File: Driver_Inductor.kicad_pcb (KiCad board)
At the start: 6 copper layers, 119.6 x 60.5 mm, 91 parts, among them J1 Control_A, J2 DC+, J3 DC-, J4 OUT1, J5 OUT2, Q1 IRLML2402TRPBF, U3 LM1117GS-5.0, U4 LMV7219M5, U5 ADuM1200AR

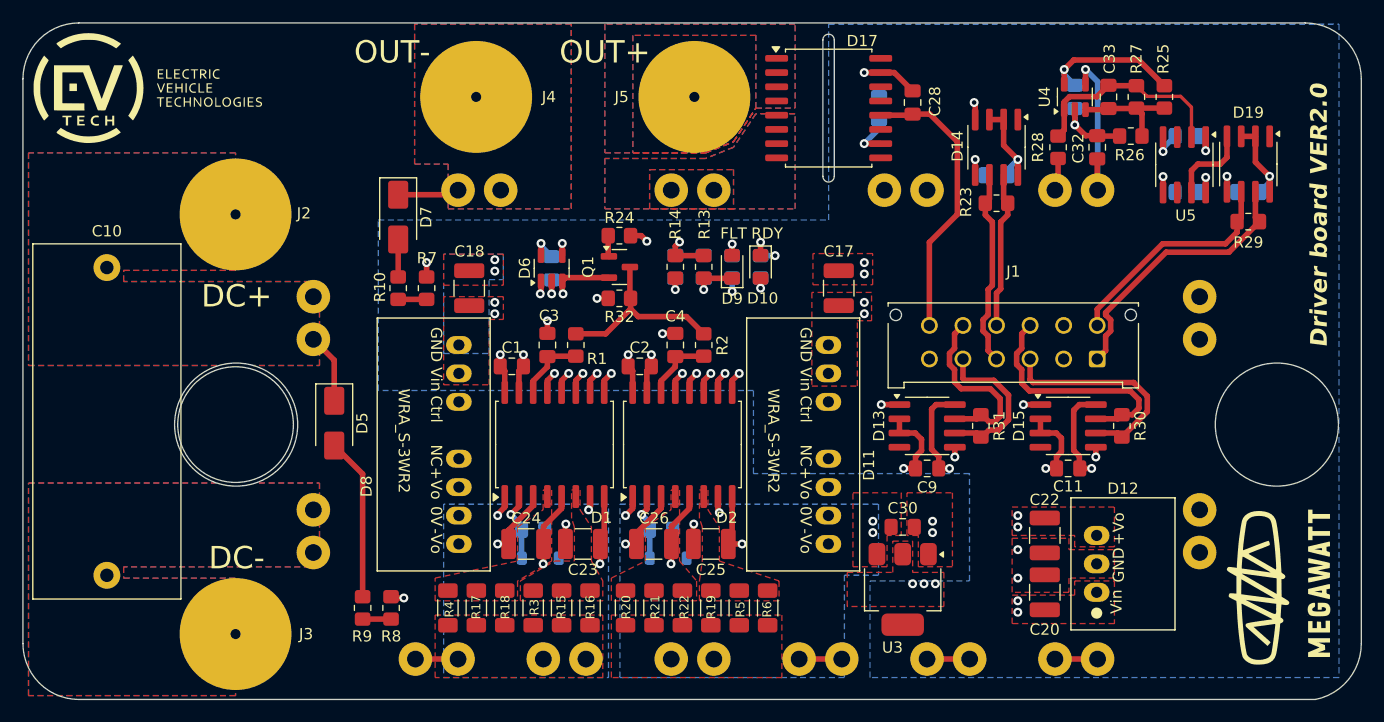
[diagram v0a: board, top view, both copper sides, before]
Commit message: VER2.1: внес все исправления для заказа в Китае
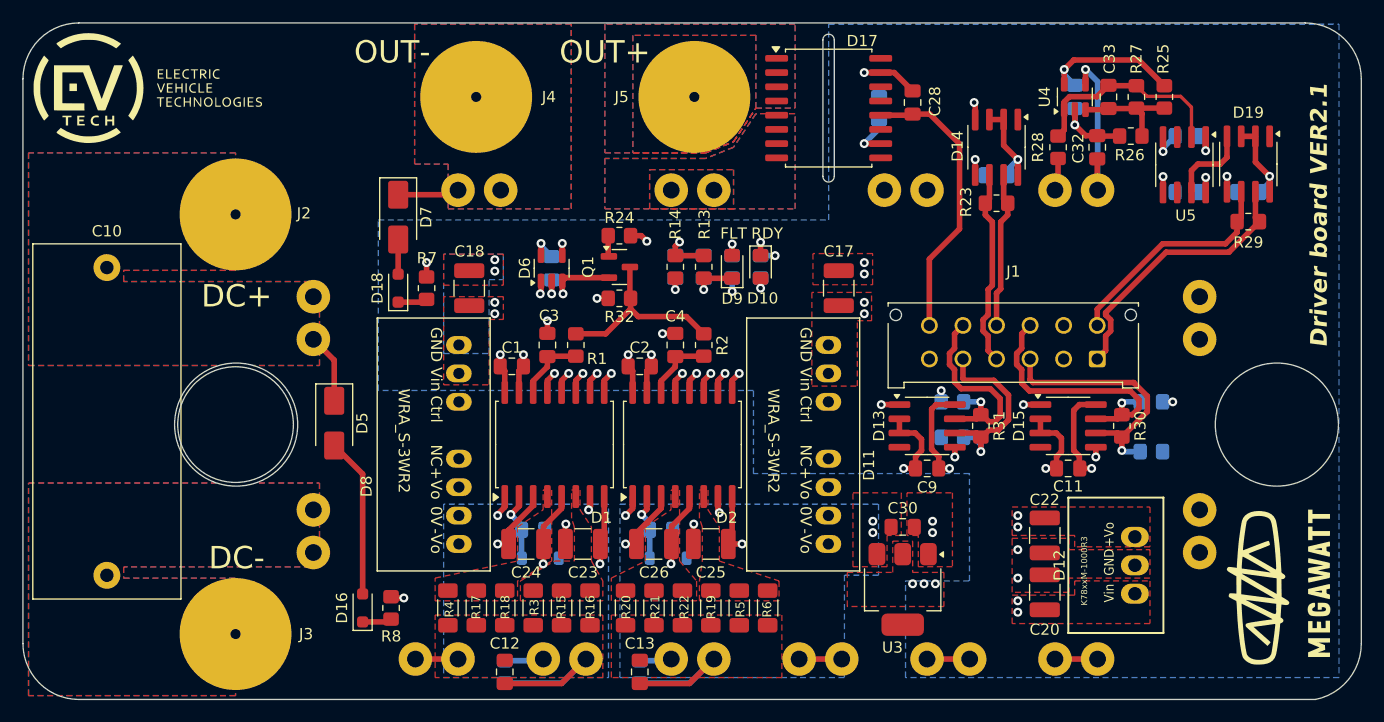
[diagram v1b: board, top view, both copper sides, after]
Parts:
- removed R10, R9: 0, Resistor_SMD:R_0805_2012Metric_Pad1.20x1.40mm_HandSolder
- added C12: 47n, Capacitor_SMD:C_0805_2012Metric_Pad1.18x1.45mm_HandSolder, F.Cu at (122.6, 119.4)
- added C13: 47n, Capacitor_SMD:C_0805_2012Metric_Pad1.18x1.45mm_HandSolder, F.Cu at (134.6, 119.4)
- added D16: 1SMB5919B, Diode_SMD:D_SOD-323_HandSoldering, F.Cu at (109.9, 113.7)
- added D18: 1SMB5919B, Diode_SMD:D_SOD-323_HandSoldering, F.Cu at (113.0, 85.1)
- added R33: 10k, Resistor_SMD:R_0805_2012Metric_Pad1.20x1.40mm_HandSolder, B.Cu at (122.6, 119.4)
- added R34: 10k, Resistor_SMD:R_0805_2012Metric_Pad1.20x1.40mm_HandSolder, B.Cu at (134.6, 119.4)
- added R35: 560, Resistor_SMD:R_0805_2012Metric_Pad1.20x1.40mm_HandSolder, B.Cu at (162.6, 95.2)
- added R36: 560, Resistor_SMD:R_0805_2012Metric_Pad1.20x1.40mm_HandSolder, B.Cu at (162.6, 98.4)
- added R37: 560, Resistor_SMD:R_0805_2012Metric_Pad1.20x1.40mm_HandSolder, B.Cu at (180.3, 95.2)
- added R38: 560, Resistor_SMD:R_0805_2012Metric_Pad1.20x1.40mm_HandSolder, B.Cu at (180.3, 99.7)
- D12: value K78xxM-1000R3 -> K7805M-1000R3; footprint Mornsun:K78xx-1000R3 -> Mornsun:K78xxM-1000R3
- D14, D19: value ADM3485E -> ADM1485JRZ
- Q1: value IRLML2402TRPBF -> BC817
- R11: value 330 -> 1k
- R12: value 330 -> 560
- R14: value 120 -> 1k
- R15, R16, R17, R18, R19, R20, R21, R22, R3, R4, R5, R6: value 10 -> 47
- R24: value 0 -> 4.7k
- R7, R8: value 10k -> 1.6k
- moved D12 1.07 mm to (178.9, 109.9)
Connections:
- net PWM1 renamed Net-(D15-RO)
- net PWM2 renamed Net-(D1-IN+)
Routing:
- net E2: track 7.92 -> 24.2 mm
- net E3: track 7.92 -> 23.0 mm
- net PWM2_P: track 14.2 -> 18.0 mm, vias 0 -> 1
- net G2: track 16.3 -> 19.8 mm
- net PWM1_P: track 20.0 -> 22.9 mm, vias 0 -> 1
- net G3: track 16.4 -> 19.2 mm
- net PWM1_N: track 21.9 -> 24.7 mm, vias 0 -> 1
- net PWM2_N: track 16.7 -> 19.4 mm, vias 0 -> 1
- net +5V: track 57.4 -> 59.3 mm, vias 14 -> 16
- net Net-(D2-DESAT): track 32.7 -> 34.1 mm
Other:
- board text added: "Driver board VER2.1"
- board text removed: "Driver board VER2.0"

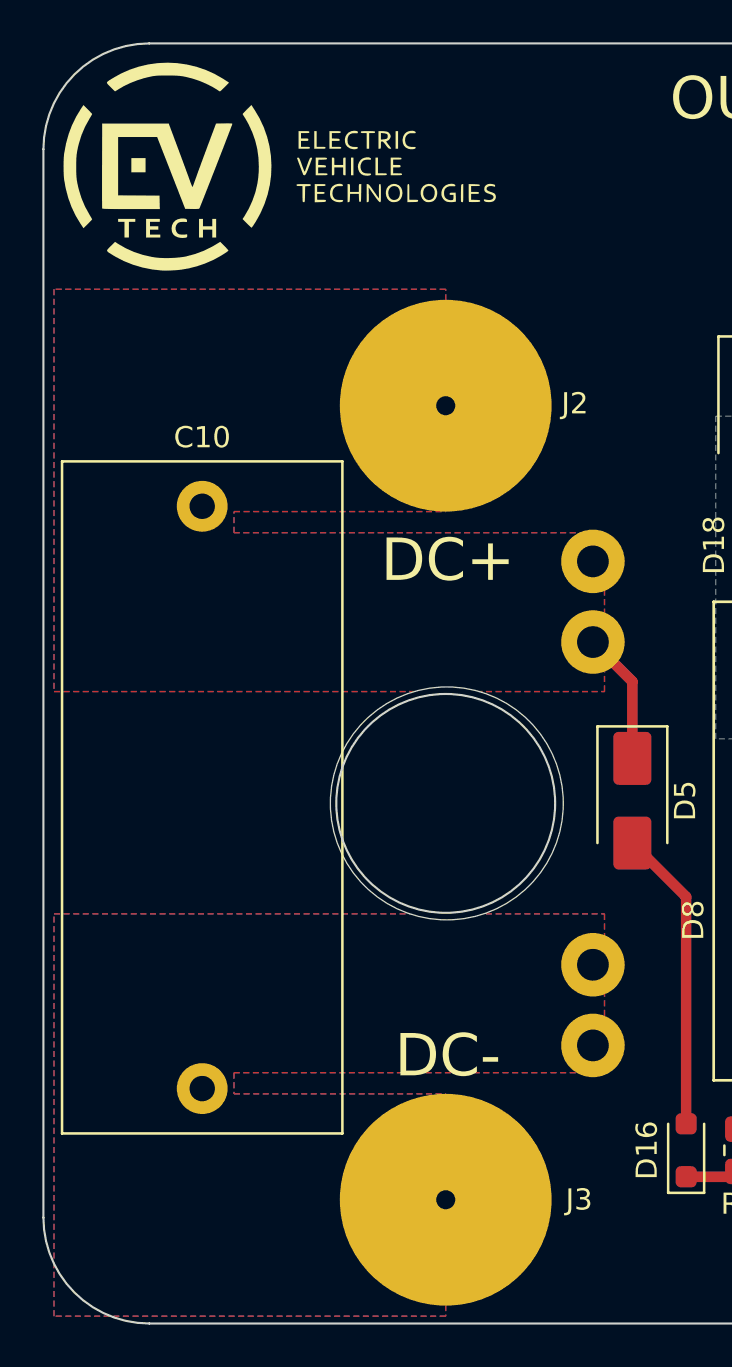
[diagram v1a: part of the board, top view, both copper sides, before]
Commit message: VER2.2: добавил цепь подавления колебаний
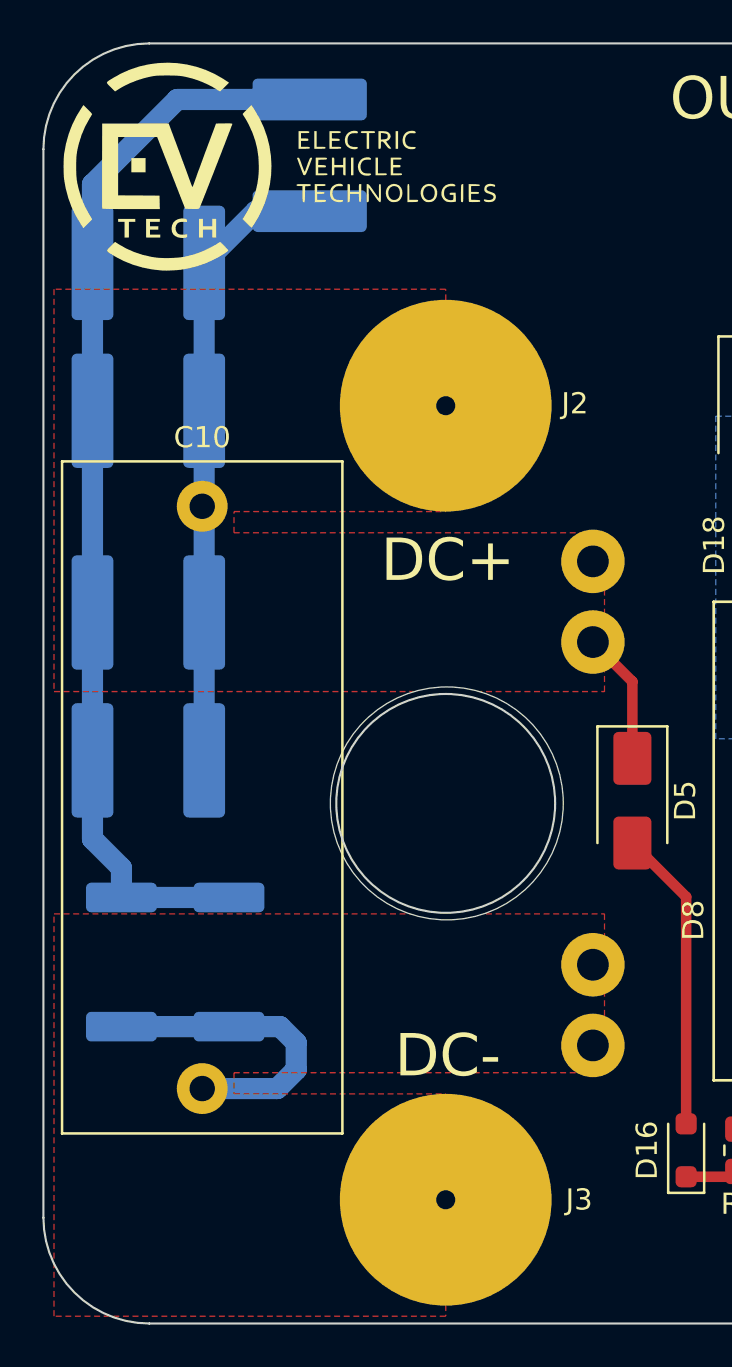
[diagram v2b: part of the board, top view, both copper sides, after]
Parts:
- added C14: 1u, Capacitor_SMD:C_2220_5750Metric_Pad1.97x5.40mm_HandSolder, B.Cu at (92.1, 66.7)
- added C19: 1u, Capacitor_SMD:C_2220_5750Metric_Pad1.97x5.40mm_HandSolder, B.Cu at (84.5, 71.8)
- added C21: 1u, Capacitor_SMD:C_2220_5750Metric_Pad1.97x5.40mm_HandSolder, B.Cu at (84.5, 78.7)
- added C29: 1u, Capacitor_SMD:C_2220_5750Metric_Pad1.97x5.40mm_HandSolder, B.Cu at (84.5, 95.2)
- added C37: 1u, Capacitor_SMD:C_2220_5750Metric_Pad1.97x5.40mm_HandSolder, B.Cu at (84.5, 88.3)
- added R10: 0.5, Resistor_SMD:R_2512_6332Metric_Pad1.40x3.35mm_HandSolder, B.Cu at (88.3, 104.8)
- added R9: 0.5, Resistor_SMD:R_2512_6332Metric_Pad1.40x3.35mm_HandSolder, B.Cu at (83.2, 104.8)
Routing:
- net Net-(C14-Pad2): track 0.00 -> 51.2 mm
- net DESAT_H: track 6.26 -> 35.8 mm
- net -VDC: track 0.00 -> 14.7 mm
- removed copper zone on B.Cu, net -VDC
- removed copper zone on B.Cu, net DESAT_H

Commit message: VER2_Test: отправил в резонит
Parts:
- moved R33 6.83 mm to (127.8, 115.0), turned to 180 degrees
- moved R34 6.34 mm to (139.2, 115.0), turned to 0 degrees
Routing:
- net E2: track 24.2 -> 19.7 mm
- net E3: track 23.0 -> 19.1 mm
- net G3: track 19.2 -> 20.1 mm
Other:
- board text added: "Driver board VER2.2"
- board text removed: "Driver board VER2.1"
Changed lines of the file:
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@@
 	(footprint "Resistor_SMD:R_0805_2012Metric_Pad1.20x1.40mm_HandSolder"
 		(layer "B.Cu")
-		(at 122.555 119.38 90)
+		(at 127.8 115 180)
 		(descr "Resistor SMD 0805 (2012 Metric), square (rectangular) end terminal, IPC_7351 nominal with elongated pad for handsoldering. (Body size source: IPC-SM-782 page 72, https://www.pcb-3d.com/wordpress/wp-content/uploads/ipc-sm-782a_amendment_1_and_2.pdf), generated with kicad-footprint-generator")
 		(tags "resistor handsolder")
 		(property "Reference" "R33"
-			(at 0 1.65 90)
+			(at 0 1.65 360)
 			(layer "B.SilkS")
 			(effects
@@
 		)
 		(property "Value" "10k"
-			(at 0 -1.65 90)
+			(at 0 -1.65 360)
 			(layer "B.Fab")
 			(effects
@@
 		)
 		(property "Footprint" "Resistor_SMD:R_0805_2012Metric_Pad1.20x1.40mm_HandSolder"
-			(at 0 0 -90)
+			(at 0 0 0)
 			(unlocked yes)
 			(layer "B.Fab")
@@
 		)
 		(property "Datasheet" ""
-			(at 0 0 -90)
+			(at 0 0 0)
 			(unlocked yes)
 			(layer "B.Fab")
@@
 		)
 		(property "Description" ""
-			(at 0 0 -90)
+			(at 0 0 0)
 			(unlocked yes)
 			(layer "B.Fab")
@@
 		(attr smd)
 		(fp_line
-			(start 0.227064 -0.735)
-			(end -0.227064 -0.735)
+			(start 0.227064 0.735)
+			(end -0.227064 0.735)
 			(stroke
 				(width 0.12)
@@
 		)
 		(fp_line
-			(start 0.227064 0.735)
-			(end -0.227064 0.735)
+			(start 0.227064 -0.735)
+			(end -0.227064 -0.735)
 			(stroke
 				(width 0.12)
@@
 		)
 		(fp_line
-			(start 1.85 -0.95)
-			(end 1.85 0.95)
+			(start 1.85 0.95)
+			(end -1.85 0.95)
 			(stroke
 				(width 0.05)
@@
 		)
 		(fp_line
-			(start -1.85 -0.95)
-			(end 1.85 -0.95)
+			(start 1.85 -0.95)
+			(end 1.85 0.95)
 			(stroke
 				(width 0.05)
@@
 		)
 		(fp_line
-			(start 1.85 0.95)
-			(end -1.85 0.95)
+			(start -1.85 0.95)
+			(end -1.85 -0.95)
 			(stroke
 				(width 0.05)
@@
 		)
 		(fp_line
-			(start -1.85 0.95)
-			(end -1.85 -0.95)
+			(start -1.85 -0.95)
+			(end 1.85 -0.95)
 			(stroke
 				(width 0.05)
@@
 		)
 		(fp_line
-			(start 1 -0.625)
-			(end 1 0.625)
+			(start 1 0.625)
+			(end -1 0.625)
 			(stroke
 				(width 0.1)
@@
 		)
 		(fp_line
-			(start -1 -0.625)
-			(end 1 -0.625)
+			(start 1 -0.625)
+			(end 1 0.625)
 			(stroke
 				(width 0.1)
@@
 		)
 		(fp_line
-			(start 1 0.625)
-			(end -1 0.625)
+			(start -1 0.625)
+			(end -1 -0.625)
 			(stroke
 				(width 0.1)
@@
 		)
 		(fp_line
-			(start -1 0.625)
-			(end -1 -0.625)
+			(start -1 -0.625)
+			(end 1 -0.625)
 			(stroke
 				(width 0.1)
@@
 		)
 		(fp_text user "${REFERENCE}"
-			(at 0 0 90)
+			(at 0 0 360)
 			(layer "B.Fab")
 			(effects
@@
 		)
 		(pad "1" smd roundrect
-			(at -1 0 90)
+			(at -1 0 180)
 			(size 1.2 1.4)
 			(layers "B.Cu" "B.Paste" "B.Mask")
@@
 		)
 		(pad "2" smd roundrect
-			(at 1 0 90)
+			(at 1 0 180)
 			(size 1.2 1.4)
 			(layers "B.Cu" "B.Paste" "B.Mask")
@@
 	(footprint "Resistor_SMD:R_0805_2012Metric_Pad1.20x1.40mm_HandSolder"
 		(layer "B.Cu")
-		(at 134.62 119.38 -90)
+		(at 139.2 115)
 		(descr "Resistor SMD 0805 (2012 Metric), square (rectangular) end terminal, IPC_7351 nominal with elongated pad for handsoldering. (Body size source: IPC-SM-782 page 72, https://www.pcb-3d.com/wordpress/wp-content/uploads/ipc-sm-782a_amendment_1_and_2.pdf), generated with kicad-footprint-generator")
 		(tags "resistor handsolder")
 		(property "Reference" "R34"
-			(at 0 1.65 90)
+			(at 0 1.65 360)
 			(layer "B.SilkS")
 			(effects
@@
 		)
 		(property "Value" "10k"
-			(at 0 -1.65 90)
+			(at 0 -1.65 360)
 			(layer "B.Fab")
 			(effects
@@
 		)
 		(property "Footprint" "Resistor_SMD:R_0805_2012Metric_Pad1.20x1.40mm_HandSolder"
-			(at 0 0 90)
+			(at 0 0 180)
 			(unlocked yes)
 			(layer "B.Fab")
@@
 		)
 		(property "Datasheet" ""
-			(at 0 0 90)
+			(at 0 0 180)
 			(unlocked yes)
 			(layer "B.Fab")
@@
 		)
 		(property "Description" ""
-			(at 0 0 90)
+			(at 0 0 180)
 			(unlocked yes)
 			(layer "B.Fab")
@@
 		(attr smd)
 		(fp_line
-			(start 0.227064 0.735)
-			(end -0.227064 0.735)
+			(start 0.227064 -0.735)
+			(end -0.227064 -0.735)
 			(stroke
 				(width 0.12)
@@
 		)
 		(fp_line
-			(start 0.227064 -0.735)
-			(end -0.227064 -0.735)
+			(start 0.227064 0.735)
+			(end -0.227064 0.735)
 			(stroke
 				(width 0.12)
@@
 		)
 		(fp_line
-			(start -1.85 0.95)
-			(end -1.85 -0.95)
+			(start -1.85 -0.95)
+			(end 1.85 -0.95)
 			(stroke
 				(width 0.05)
@@
 		)
 		(fp_line
-			(start 1.85 0.95)
-			(end -1.85 0.95)
+			(start -1.85 0.95)
+			(end -1.85 -0.95)
 			(stroke
 				(width 0.05)
@@
 		)
 		(fp_line
-			(start -1.85 -0.95)
-			(end 1.85 -0.95)
+			(start 1.85 -0.95)
+			(end 1.85 0.95)
 			(stroke
 				(width 0.05)
@@
 		)
 		(fp_line
-			(start 1.85 -0.95)
-			(end 1.85 0.95)
+			(start 1.85 0.95)
+			(end -1.85 0.95)
 			(stroke
 				(width 0.05)
@@
 		)
 		(fp_line
-			(start -1 0.625)
-			(end -1 -0.625)
+			(start -1 -0.625)
+			(end 1 -0.625)
 			(stroke
 				(width 0.1)
@@
 		)
 		(fp_line
-			(start 1 0.625)
-			(end -1 0.625)
+			(start -1 0.625)
+			(end -1 -0.625)
 			(stroke
 				(width 0.1)
@@
 		)
 		(fp_line
-			(start -1 -0.625)
-			(end 1 -0.625)
+			(start 1 -0.625)
+			(end 1 0.625)
 			(stroke
 				(width 0.1)
@@
 		)
 		(fp_line
-			(start 1 -0.625)
-			(end 1 0.625)
+			(start 1 0.625)
+			(end -1 0.625)
 			(stroke
 				(width 0.1)
@@
 		)
 		(fp_text user "${REFERENCE}"
-			(at 0 0 90)
+			(at 0 0 360)
 			(layer "B.Fab")
 			(effects
@@
 		)
 		(pad "1" smd roundrect
-			(at -1 0 270)
+			(at -1 0)
 			(size 1.2 1.4)
 			(layers "B.Cu" "B.Paste" "B.Mask")
@@
 		)
 		(pad "2" smd roundrect
-			(at 1 0 270)
+			(at 1 0)
 			(size 1.2 1.4)
 			(layers "B.Cu" "B.Paste" "B.Mask")
@@
 		(tags "capacitor handsolder")
 		(property "Reference" "C37"
-			(at 0 0 360)
+			(at 0 0 0)
 			(layer "B.SilkS")
 			(effects
@@
 		)
 		(property "Value" "1u"
-			(at 0 -3.65 360)
+			(at 0 -3.65 0)
 			(layer "B.Fab")
 			(effects
@@
 		)
 		(fp_text user "${REFERENCE}"
-			(at 0 0 360)
+			(at 0 0 0)
 			(layer "B.Fab")
 			(effects
@@
 		(tags "capacitor handsolder")
 		(property "Reference" "C29"
-			(at 0 0 360)
+			(at 0 0 0)
 			(layer "B.SilkS")
 			(effects
@@
 		)
 		(property "Value" "1u"
-			(at 0 -3.65 360)
+			(at 0 -3.65 0)
 			(layer "B.Fab")
 			(effects
@@
 		)
 		(fp_text user "${REFERENCE}"
-			(at 0 0 360)
+			(at 0 0 0)
 			(layer "B.Fab")
 			(effects
@@
 		)
 	)
-	(gr_text "Driver board VER2.1"
+	(gr_text "Driver board VER2.2\n"
 		(at 196.2 90.4 90)
 		(layer "F.SilkS")
@@
 	)
 	(segment
-		(start 122.555 120.38)
-		(end 127.664 120.38)
+		(start 129.812 116.012)
+		(end 128.8 115)
 		(width 0.5)
 		(layer "B.Cu")
@@
 	)
 	(segment
-		(start 127.664 120.38)
-		(end 129.812 118.232)
+		(start 129.812 118.232)
+		(end 129.812 116.012)
 		(width 0.5)
 		(layer "B.Cu")
@@
 	)
 	(segment
-		(start 122.555 118.38)
-		(end 125.854 118.38)
+		(start 126.002 118.232)
+		(end 126.002 115.798)
+		(width 0.5)
+		(layer "B.Cu")
+		(net 15)
+	)
+	(segment
+		(start 126.002 115.798)
+		(end 126.8 115)
 		(width 0.5)
 		(layer "B.Cu")
@@
 	)
 	(segment
+		(start 137.432 118.232)
+		(end 137.432 115.768)
+		(width 0.5)
+		(layer "B.Cu")
+		(net 34)
+	)
+	(segment
 		(start 137.284 118.38)
 		(end 137.432 118.232)
@@
 	)
 	(segment
-		(start 134.62 118.38)
-		(end 137.284 118.38)
+		(start 137.432 115.768)
+		(end 138.2 115)
 		(width 0.5)
 		(layer "B.Cu")
@@
 	)
 	(segment
-		(start 134.62 120.38)
-		(end 139.094 120.38)
+		(start 141.242 116.042)
+		(end 140.2 115)
 		(width 0.5)
 		(layer "B.Cu")
@@
 	)
 	(segment
-		(start 139.094 120.38)
-		(end 141.242 118.232)
+		(start 141.242 118.232)
+		(end 141.242 116.042)
 		(width 0.5)
 		(layer "B.Cu")

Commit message: VER2_Test: добавил новый BOM и в схеме заменил названия компонентов
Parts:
- C5, C6: value 220p -> 100p
- D13, D14, D15, D19: value ADM1485JRZ -> SN65HVD3082EDR
- U5: value ADuM1200AR -> SCM3728ASA
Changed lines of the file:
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@@
 			)
 		)
-		(property "Value" "ADM1485JRZ"
+		(property "Value" "SN65HVD3082EDR"
 			(at 0 3.4 0)
 			(layer "F.Fab")
@@
 			)
 		)
-		(property "Value" "ADuM1200AR"
+		(property "Value" "SCM3728ASA"
 			(at -0.27 -3.6688 90)
 			(layer "F.Fab")
@@
 			)
 		)
-		(property "Value" "ADM1485JRZ"
+		(property "Value" "SN65HVD3082EDR"
 			(at 0 3.4 90)
 			(layer "F.Fab")
@@
 			)
 		)
-		(property "Value" "ADM1485JRZ"
+		(property "Value" "SN65HVD3082EDR"
 			(at 0 3.4 0)
 			(layer "F.Fab")
@@
 			)
 		)
-		(property "Value" "ADM1485JRZ"
+		(property "Value" "SN65HVD3082EDR"
 			(at -0.0142 4.4562 90)
 			(layer "F.Fab")
@@
 			)
 		)
-		(property "Value" "220p"
+		(property "Value" "100p"
 			(at 0 -1.68 0)
 			(layer "B.Fab")
@@
 			)
 		)
-		(property "Value" "220p"
+		(property "Value" "100p"
 			(at 0 -1.68 0)
 			(layer "B.Fab")
@@
 		(tags "resistor handsolder")
 		(property "Reference" "R33"
-			(at 0 1.65 360)
+			(at 0 1.65 0)
 			(layer "B.SilkS")
 			(effects
@@
 		)
 		(property "Value" "10k"
-			(at 0 -1.65 360)
+			(at 0 -1.65 0)
 			(layer "B.Fab")
 			(effects
@@
 		)
 		(fp_text user "${REFERENCE}"
-			(at 0 0 360)
+			(at 0 0 0)
 			(layer "B.Fab")
 			(effects
@@
 		(tags "resistor handsolder")
 		(property "Reference" "R34"
-			(at 0 1.65 360)
+			(at 0 1.65 0)
 			(layer "B.SilkS")
 			(effects
@@
 		)
 		(property "Value" "10k"
-			(at 0 -1.65 360)
+			(at 0 -1.65 0)
 			(layer "B.Fab")
 			(effects
@@
 		)
 		(fp_text user "${REFERENCE}"
-			(at 0 0 360)
+			(at 0 0 0)
 			(layer "B.Fab")
 			(effects

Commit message: VER2_Test: сделал схему в один лист красиво
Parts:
- D19: value SN65HVD3082EDR -> ADM3485E
